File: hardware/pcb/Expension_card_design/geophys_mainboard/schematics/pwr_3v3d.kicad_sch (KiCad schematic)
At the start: 32 parts, among them Q2 AO3401A, Q3 AO3400A, U10 TPS54331DR, U9 TPS2116DRL

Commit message: SCL3300 driver functionnal
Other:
- note added: "enlever D9"
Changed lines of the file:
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@@
+		)
+	)
+	(text "enlever D9"
+		(exclude_from_sim no)
+		(at 112.522 148.844 0)
+		(effects
+			(font
+				(size 1.27 1.27)
+			)
 		)
 	)

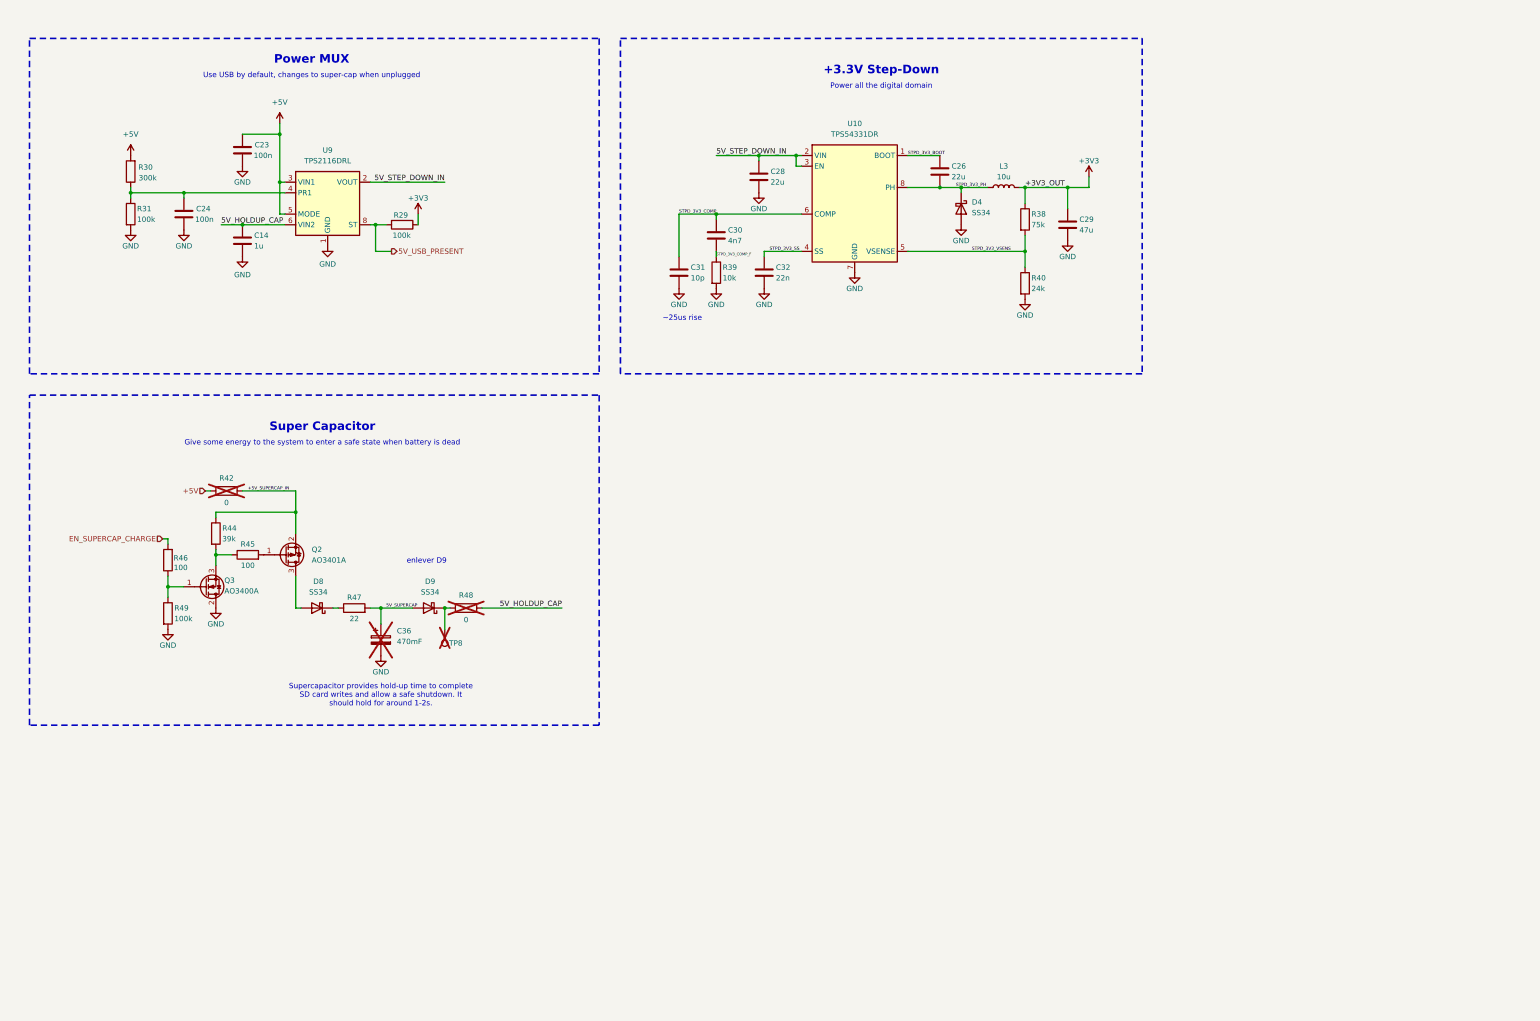
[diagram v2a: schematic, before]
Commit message: Backup avant deletion offset/dac
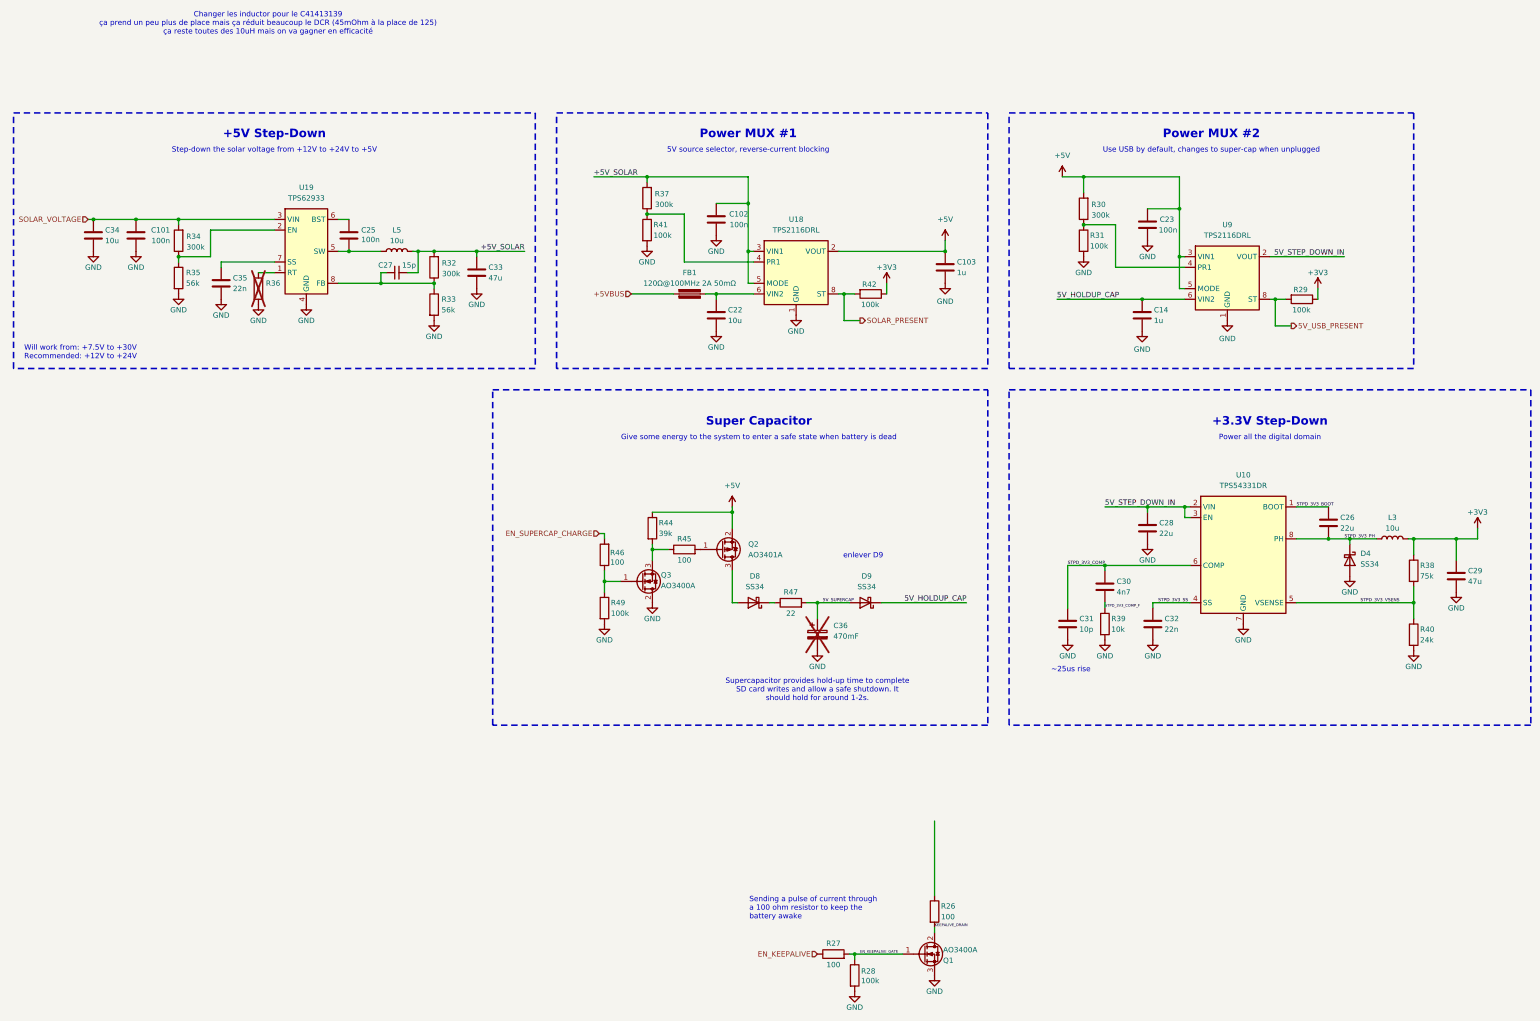
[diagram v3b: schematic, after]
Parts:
- removed C24: 100n, Capacitor_SMD:C_0603_1608Metric, symbol Device:C
- removed R48: 0, Resistor_SMD:R_1206_3216Metric, symbol Device:R
- removed TP8: TestPoint, TestPoint:TestPoint_THTPad_1.0x1.0mm_Drill0.5mm, symbol Connector:TestPoint
- added C101, C102, C25: 100n, Capacitor_SMD:C_0603_1608Metric, symbol Device:C
- added C103: 1u, Capacitor_SMD:C_0805_2012Metric, symbol Device:C
- added C22, C34: 10u, Capacitor_SMD:C_0805_2012Metric, symbol Device:C
- added C27: 15p, Capacitor_SMD:C_0603_1608Metric, symbol Device:C_Small
- added C33: 47u, Capacitor_SMD:C_1206_3216Metric, symbol Device:C
- added C35: 22n, Capacitor_SMD:C_0603_1608Metric, symbol Device:C
- added FB1: 120Ω@100MHz 2A 50mΩ, Inductor_SMD:L_0603_1608Metric, symbol PCM_Device_AKL:Ferrite_Bead
- added L5: 10u, magnode_footprints:ZEMS0850-100M_8.5x8.0mm, symbol Device:L
- added Q1: AO3400A, Package_TO_SOT_SMD:SOT-23, symbol magnode_symbols:AO3400A
- added R26, R27: 100, Resistor_SMD:R_0603_1608Metric, symbol Device:R
- added R28, R41: 100k, Resistor_SMD:R_0603_1608Metric, symbol Device:R
- added R32, R34, R37: 300k, Resistor_SMD:R_0603_1608Metric, symbol Device:R
- added R33, R35: 56k, symbol Device:R
- added R36: ~, Resistor_SMD:R_0603_1608Metric, symbol Device:R
- added U18: TPS2116DRL, Package_TO_SOT_SMD:SOT-583-8, symbol Power_Management:TPS2116DRL
- added U19: TPS62933, Package_TO_SOT_SMD:SOT-583-8, symbol Regulator_Switching:TPS62933
- L3: footprint Inductor_SMD:L_Sunlord_MWSA0503S -> magnode_footprints:ZEMS0850-100M_8.5x8.0mm; LCSC C177248 -> C41413139
- R42: value 0 -> 100k; footprint Resistor_SMD:R_1206_3216Metric -> Resistor_SMD:R_0603_1608Metric; LCSC C17888 -> C25803; now fitted
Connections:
- net +3V3: now also R42.1
- net +5V: now also Q2.2, R44.1, C103.1, U18.2 (VOUT), U18.7 (VOUT); no longer R42.1
- net 5V_HOLDUP_CAP: now also D9.1 (K)
- net GND: now also C101.1, C102.1, C103.2, C22.2, C33.2, C34.2, C35.2, Q1.3, R28.2, R33.2, R35.2, R36.2, R41.2, U18.1 (GND), U19.4 (GND)
- removed net +5V_SUPERCAP_IN: Q2.2, R42.2, R44.1
- new net: C22.1, FB1.2, U18.6 (VIN2)
- new net: R37.1, R41.1, U18.4 (PR1)
- new net: C25.1, L5.1, U19.5 (SW)
- new net: C25.2, U19.6 (BST)
- new net: R34.1, R35.1, U19.2 (EN)
- new net: C27.1, R32.1, R33.1, U19.8 (FB)
- new net: R36.1, U19.1 (RT)
- new net: C35.1, U19.7 (SS)
- new net +5VBUS: FB1.1
- new net +5V_SOLAR: C102.2, C27.2, C33.1, L5.2, R32.2, R37.2, U18.3 (VIN1), U18.5 (MODE)
- new net EN_KEEPALIVE: R27.1
- new net EN_KEEPALIVE_GATE: Q1.1, R27.2, R28.1
- new net KEEPALIVE_DRAIN: Q1.2, R26.2
- new net SOLAR_PRESENT: R42.2, U18.8 (ST)
- new net SOLAR_VOLTAGE: C101.2, C34.1, R34.2, U19.3 (VIN)
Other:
- note added: "+5V Step-Down"
- note added: "5V source selector, reverse-current blocking"
- note added: "Changer les inductor pour le C41413139 ça prend un peu plus de place mais ça réduit beaucoup le DCR (45mOhm à la place de 125) ça reste toutes des 10uH mais on va gagner en efficacité"
- note added: "Power MUX #1"
- note added: "Power MUX #2"
- note added: "Sending a pulse of current through a 100 ohm resistor to keep the battery awake"
- note added: "Step-down the solar voltage from +12V to +24V to +5V"
- note added: "Will work from: +7.5V to +30V Recommended: +12V to +24V"
- note removed: "Power MUX"
- moved on the sheet: C14, C23, C26, C28, C29, C30, C31, C32, C36, D4, D8, D9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

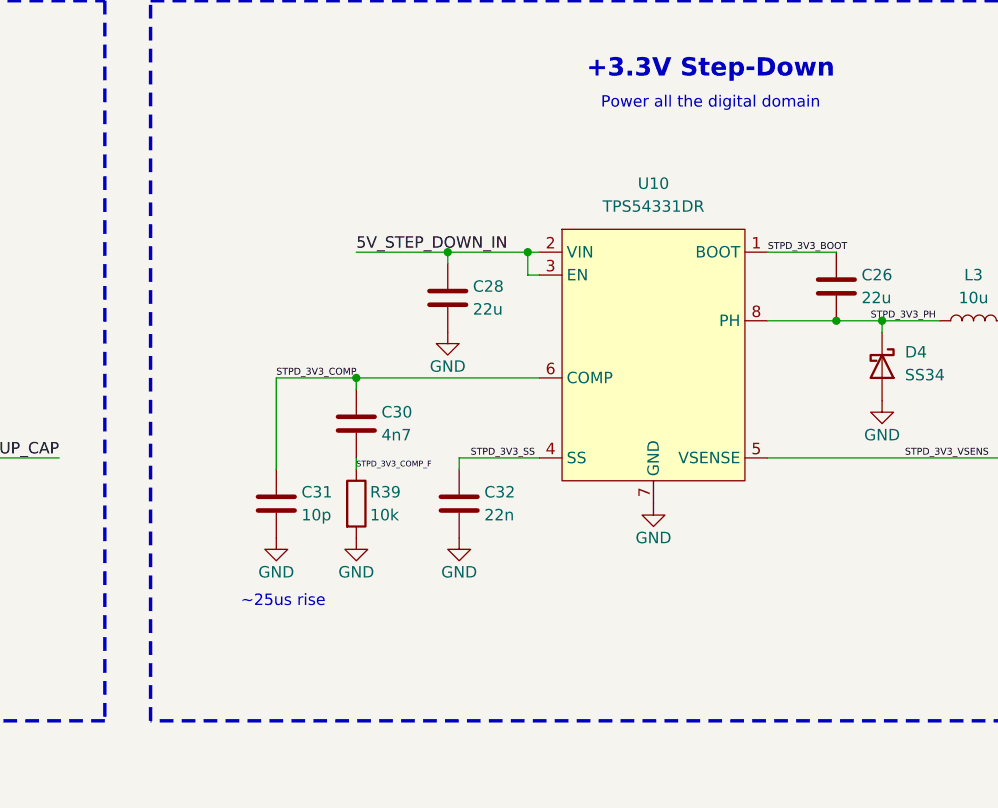
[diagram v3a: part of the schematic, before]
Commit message: SD mux and 3V3D power sequencing bring-up
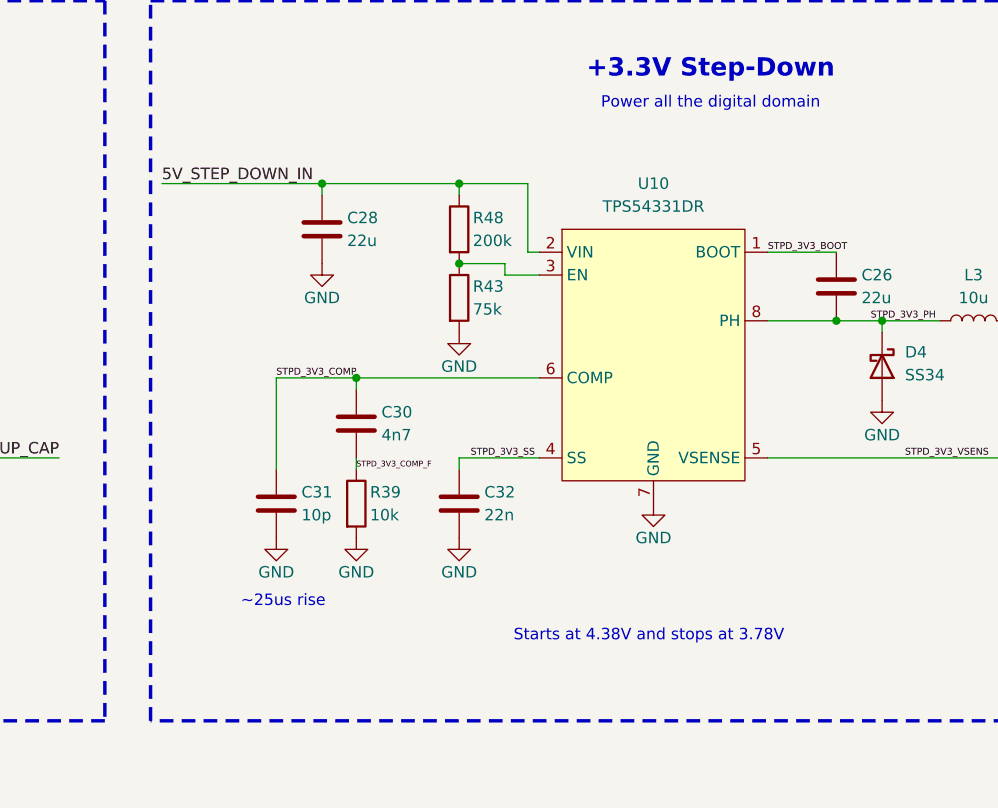
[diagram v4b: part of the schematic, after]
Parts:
- added R43: 75k, Resistor_SMD:R_0603_1608Metric, symbol Device:R
- added R48: 200k, Resistor_SMD:R_0603_1608Metric, symbol Device:R
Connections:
- net 5V_STEP_DOWN_IN: now also R48.1; no longer U10.3 (EN)
- net GND: now also R43.2
- new net: R43.1, R48.2, U10.3 (EN)
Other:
- note added: "Starts at 4.38V and stops at 3.78V"
- moved on the sheet: C28

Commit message: Work in progress rev2
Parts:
- removed Q1: AO3400A, Package_TO_SOT_SMD:SOT-23, symbol magnode_symbols:AO3400A
- removed R26, R27: 100, Resistor_SMD:R_0603_1608Metric, symbol Device:R
- removed R28: 100k, Resistor_SMD:R_0603_1608Metric, symbol Device:R
- added C10, C37, C40, C6, C79, C80, C81, C82, C9: 4u7, Capacitor_SMD:C_1206_3216Metric, symbol Device:C
- added C38, C39, C69, C72, C76, C8: 100n, Capacitor_SMD:C_0603_1608Metric, symbol Device:C
- added C4: 22p, Capacitor_SMD:C_0603_1608Metric, symbol Device:C
- added C5: 1u, Capacitor_SMD:C_0805_2012Metric, symbol Device:C
- added C65, C67, C7, C71, C77: 10u, Capacitor_SMD:C_0805_2012Metric, symbol Device:C
- added C66, C68, C73, C78: 10n, Capacitor_SMD:C_0603_1608Metric, symbol Device:C
- added C70: 220n, Capacitor_SMD:C_0603_1608Metric, symbol Device:C
- added C74: 47u, Capacitor_SMD:C_1206_3216Metric, symbol Device:C
- added C75: 10p, Capacitor_SMD:C_0603_1608Metric, symbol Device:C
- added C83: 4n7, Capacitor_SMD:C_0603_1608Metric, symbol Device:C
- added D10, D2: SS34, Diode_SMD:D_SMA, symbol Device:D_Schottky
- added L2, L4: 10u, magnode_footprints:ZEMS0850-100M_8.5x8.0mm, symbol Device:L
- added R12, R92: 510k, Resistor_SMD:R_0603_1608Metric, symbol Device:R
- added R13: 1k, Resistor_SMD:R_0603_1608Metric, symbol Device:R
- added R14: 200k, Resistor_SMD:R_0603_1608Metric, symbol Device:R
- added R16: 90k9, Resistor_SMD:R_1206_3216Metric, symbol Device:R
- added R17, R87, R90, R93: 100k, Resistor_SMD:R_0603_1608Metric, symbol Device:R
- added R83: 39k, Resistor_SMD:R_0603_1608Metric, symbol Device:R
- added R84: 12k, Resistor_SMD:R_0603_1608Metric, symbol Device:R
- added R88: 330k, Resistor_SMD:R_0603_1608Metric, symbol Device:R
- added R89: 10, Resistor_SMD:R_0603_1608Metric, symbol Device:R
- added U11: TPS7A2033PDBVR, Package_TO_SOT_SMD:SOT-23-5, symbol magnode_symbols:TPS7A2033PDBVR
- added U13: TPS7A4901DGNR, magnode_footprints:HVSSOP-8-1EP_3x3mm_P0.65mm_EP1.57x1.89mm, symbol magnode_symbols:TPS7A4901
- added U14: TPS7A3301RGWR, Package_DFN_QFN:Texas_RGW0020A_VQFN-20-1EP_5x5mm_P0.65mm_EP3.15x3.15mm, symbol Regulator_Linear:TPS7A3301RGW
- added U15: TPS63700DRCR, Package_SON:VSON-10-1EP_3x3mm_P0.5mm_EP1.2x2mm, symbol magnode_symbols:TPS63700
- added U2: LT3042xMSE, Package_SO:MSOP-10-1EP_3x3mm_P0.5mm_EP1.68x1.88mm, symbol Regulator_Linear:LT3042xMSE
- added U3: TPS61040DBV, Package_TO_SOT_SMD:SOT-23-5, symbol Regulator_Switching:TPS61040DBV
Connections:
- net +5V: now also C10.1, C37.1, C38.1, C77.1, L2.1, R89.2, U11.1 (IN), U15.5 (IN), U3.5 (VIN)
- net GND: now also C10.2, C37.2, C38.2, C39.2, C40.2, C5.2, C6.2, C65.2, C67.2, C68.2, C69.2, C7.2, C70.2, C71.2, C72.2, C74.2, C76.2, C77.2, C78.2, C79.2, C8.2, C80.2, C81.2, C82.2, C83.2, C9.2, L4.2, R13.1, R16.2, R17.2, R84.2, R90.2, U11.2 (GND), U11.4 (NC), U13.3 (NC), U13.4 (GND), U13.9 (PwPd), U14.21 (EP), U14.7 (GND), U15.11 (PowerPAD), U15.2 (GND), U15.7 (PSGND), U2.11 (GND), U2.8 (GND), U3.2 (GND)
- new net +10V: C4.1, C5.1, C65.1, C7.1, C8.1, D2.1 (K), R12.1, U13.5 (EN), U13.8 (IN), U2.1 (IN), U2.2 (IN), U2.3 (EN/UV), U2.6 (PGFB)
- new net +3V3A: C39.1, C40.1, U11.5 (OUT)
- new net +5VA: C66.1, C67.1, R83.1, U13.1 (OUT)
- new net +9VA: C6.1, U2.10 (OUT), U2.9 (OUTS)
- new net -5VA: C73.1, C74.1, R88.1, U14.1 (OUT), U14.20 (OUT)
- new net -6V2: C71.1, C72.1, C78.1, C79.1, C80.1, C81.1, C82.1, D10.2 (A), R92.2, R93.2, U14.13 (EN), U14.15 (IN), U14.16 (IN), U15.8 (OUT)
- new net BST_10V_FB: C4.2, R14.2, R17.1, U3.3 (FB)
- new net BST_10V_FB_DIV: R12.2, R14.1
- new net BST_10V_SW: D2.2 (A), L2.2, U3.1 (SW)
- new net EN_BST_10V: U3.4 (EN)
- new net EN_INV_-5V: U15.4 (EN)
- new net EN_LDO_3V3: U11.3 (EN)
- new net INV_N5V5_COMP: C83.1, U15.1 (COMP)
- new net INV_N5V5_FB: C75.1, R87.2, R92.1, U15.9 (FB)
- new net INV_N5V5_FF: C75.2, R93.1
- new net INV_N5V5_SW: D10.1 (K), L4.1, U15.6 (SW)
- new net INV_N5V5_VIN: C69.1, R89.1, U15.3 (VIN)
- new net INV_N5V5_VREF: C70.1, R87.1, U15.10 (VREF)
- new net LDO_9V_ILIM: R13.2, U2.5 (ILIM)
- new net LDO_9V_SET: C9.1, R16.1, U2.7 (SET)
- new net LDO_N5V_FB: C73.2, R88.2, R90.1, U14.3 (FB)
- new net LDO_N5V_NR: C76.1, U14.14 (NR/SS)
- new net LDO_P5V_FB: C66.2, R83.2, R84.1, U13.2 (FB)
- new net LDO_P5V_NR: C68.1, U13.6 (NR/SS)
- no-connect marks 0 -> 2
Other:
- note added: "+10V Boost"
- note added: "+3.3V LDO"
- note added: "+5V LDO"
- note added: "+9V LDO"
- note added: "-5V LDO"
- note added: "-6.2V Inverter"
- note added: "Voltage for analog domain of the ADC"
- note added: "Voltage for bridge of the magnetic sensors"
- note added: "Voltage for the +9V and +5V LDO"
- note added: "Voltage for the instrumentation Op-Amps"
- note added: "Voltage needed for the -5V LDO"
- note removed: "Sending a pulse of current through a 100 ohm resistor to keep the battery awake"
- moved on the sheet: C14, C23, R29, R30, R31, U9
